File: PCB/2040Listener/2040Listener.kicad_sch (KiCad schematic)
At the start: 33 parts, among them J1 CONN4_292303_SOCKET, J2 USB-AP-S-RA-PLUG, SW1 PTS815 SJM 250 SMTR LFS, SW2 PTS815 SJM 250 SMTR LFS, U1 RP2040, U2 NCP1117-3.3_SOT223, U4 BY25Q16AWTIG(R), Y1 ABM8-272-T3

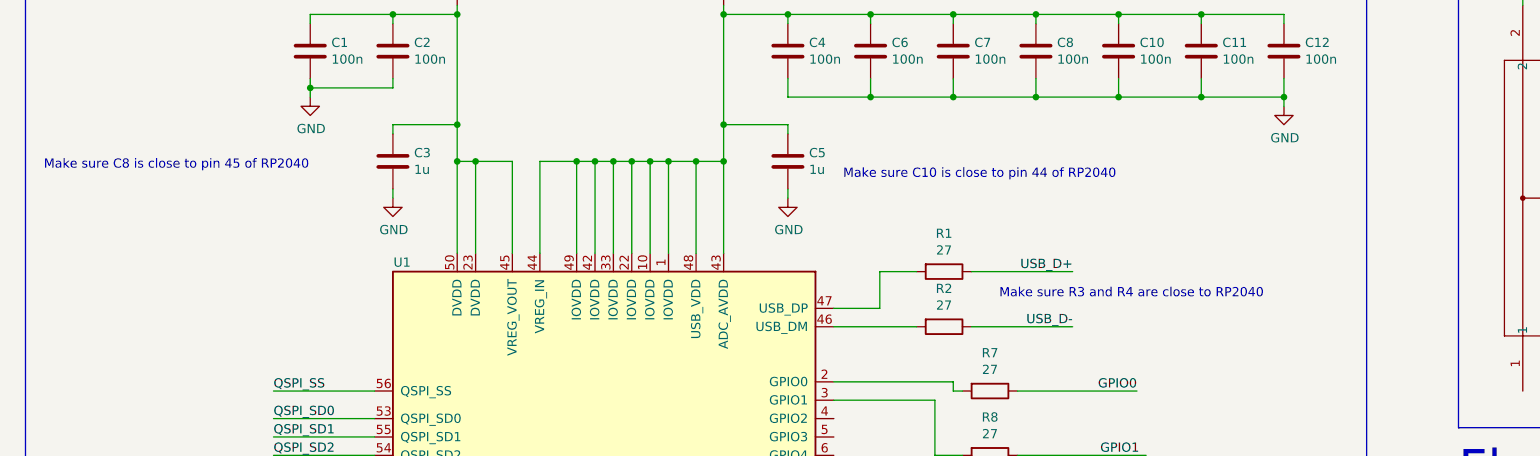
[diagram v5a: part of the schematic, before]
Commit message: update schematic text
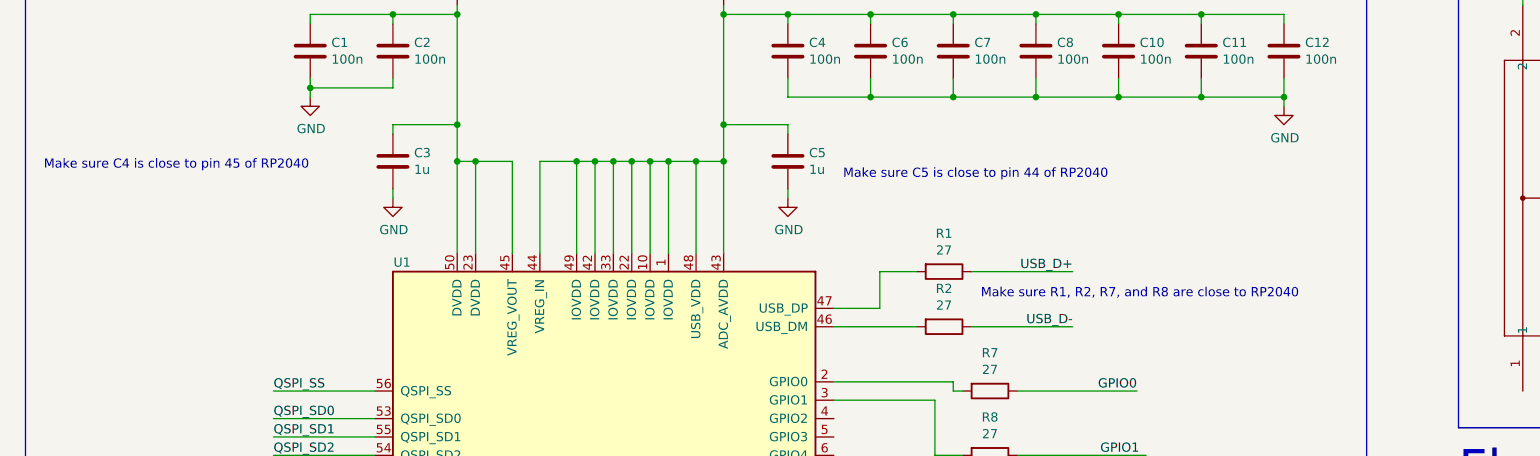
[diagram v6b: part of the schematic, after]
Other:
- note added: "Make sure C4 is close to pin 45 of RP2040"
- note added: "Make sure C5 is close to pin 44 of RP2040"
- note added: "Make sure R1, R2, R7, and R8 are close to RP2040"
- note removed: "Make sure C10 is close to pin 44 of RP2040"
- note removed: "Make sure C8 is close to pin 45 of RP2040"
- note removed: "Make sure R3 and R4 are close to RP2040"
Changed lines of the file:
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@@
 		)
 	)
-	(text "Make sure C10 is close to pin 44 of RP2040"
+	(text "Make sure C5 is close to pin 44 of RP2040"
 		(exclude_from_sim no)
 		(at 130.81 45.72 0)
@@
 		)
 	)
-	(text "Make sure R3 and R4 are close to RP2040"
+	(text "Make sure R1, R2, R7, and R8 are close to RP2040"
 		(exclude_from_sim no)
-		(at 152.4 62.23 0)
+		(at 149.86 62.23 0)
 		(effects
 			(font
@@
 		)
 	)
-	(text "Make sure C8 is close to pin 45 of RP2040"
+	(text "Make sure C4 is close to pin 45 of RP2040"
 		(exclude_from_sim no)
 		(at 20.32 44.45 0)

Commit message: update pcb spacing
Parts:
- added C18, C19, C20, C21, C22: 10u, Capacitor_SMD:C_0805_2012Metric, symbol Device:C
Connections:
- net +3V3: now also C22.1
- net GND: now also C18.2, C19.2, C20.2, C21.2, C22.2
- net VBUS: now also C18.1, C19.1, C20.1, C21.1
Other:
- note added: "BULK (OPTIONAL)"
- note added: "BULK + DECOUPLE"
- note added: "C22 OPTIONAL"
